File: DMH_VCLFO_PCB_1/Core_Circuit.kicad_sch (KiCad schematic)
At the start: 0 parts

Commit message: schematic design in progress
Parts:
- added C5: 1uF, Capacitor_THT:C_Disc_D4.3mm_W1.9mm_P5.00mm, symbol Device:C
- added C6: 100nF, Capacitor_THT:C_Disc_D4.3mm_W1.9mm_P5.00mm, symbol Device:C
- added C7: 10nF, Capacitor_THT:C_Disc_D4.3mm_W1.9mm_P5.00mm, symbol Device:C
- added C8: 100pF, Capacitor_THT:C_Disc_D4.3mm_W1.9mm_P5.00mm, symbol Device:C
- added D3, D4: 1N4148, Diode_THT:D_DO-35_SOD27_P7.62mm_Horizontal, symbol Diode:1N4148
- added J1, J2: TS_Jack_6.35mm_Sw, SynthStuff:CUI_MJ-63052A, symbol SynthStuff:TS_Jack_6.35mm_Sw
- added Q1: BS170, Package_TO_SOT_THT:TO-92_Inline, symbol Transistor_FET:BS170
- added Q2, Q3: BC548, Package_TO_SOT_THT:TO-92L_Inline_Wide, symbol Transistor_BJT:BC548
- added R1: 270R, Resistor_THT:R_Axial_DIN0207_L6.3mm_D2.5mm_P7.62mm_Horizontal, symbol Device:R_US
- added R10, R16, R8, R9: 51k, Resistor_THT:R_Axial_DIN0207_L6.3mm_D2.5mm_P7.62mm_Horizontal, symbol Device:R_US
- added R11, R17: 47k, Resistor_THT:R_Axial_DIN0207_L6.3mm_D2.5mm_P7.62mm_Horizontal, symbol Device:R_US
- added R12, R14, R15: 10k, Resistor_THT:R_Axial_DIN0207_L6.3mm_D2.5mm_P7.62mm_Horizontal, symbol Device:R_US
- added R13: 3k9, Resistor_THT:R_Axial_DIN0207_L6.3mm_D2.5mm_P7.62mm_Horizontal, symbol Device:R_US
- added R18, R19, R2, R20, R4, R5, R6, R7: 100k, Resistor_THT:R_Axial_DIN0207_L6.3mm_D2.5mm_P7.62mm_Horizontal, symbol Device:R_US
- added R3: 33k, Resistor_THT:R_Axial_DIN0207_L6.3mm_D2.5mm_P7.62mm_Horizontal, symbol Device:R_US
- added RV1: 50k, Potentiometer_THT:Potentiometer_Bourns_3296X_Horizontal, symbol Device:R_Potentiometer_Trim_US
- added RV1, RV2: B100k, SynthStuff:Potentiometer_TT_P110KH1, symbol Device:R_Potentiometer_US
- added SW1: SW_SPDT, symbol Switch:SW_SPDT
- added U1: TL074, Package_DIP:DIP-14_W7.62mm_Socket, symbol Amplifier_Operational:TL074
- added U2, U7: TL072, Package_DIP:DIP-8_W7.62mm_Socket, symbol Amplifier_Operational:TL072
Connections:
- new net: Q1.1 (D), R9.2
- new net: Q1.2 (G), R13.1, R14.1
- new net: C7.1, J2.T, R11.1
- new net: R15.1, R16.1, U1.5 (+)
- new net: C5.2, C6.2, R18.1, R19.1, U1.1, U1.6 (-)
- new net: D4.2 (A), R14.2, R15.2, U1.7
- new net: R2.1, R4.1, U1.13 (-)
- new net: R4.2, R7.1, R8.1, U1.14
- new net: D4.1 (K), R17.1
- new net: Q3.2 (B), R17.2
- new net: C7.2, D3.1 (K), R12.1
- new net: Q2.2 (B), R12.2
- new net: R10.1, R8.2, U1.3 (+)
- new net: Q3.1 (C), R18.2, U2.3 (+)
- new net: C6.1, Q2.1 (C), R7.2, R9.1, SW1.2 (B), U1.2 (-)
- new net: J1.T, R3.1, RV2.3
- new net: R3.2, RV1.1, U7.2 (-)
- new net: R6.2, RV1.2, RV1.3, U7.1
- new net: R5.2, R6.1, U1.12 (+)
- new net: R1.1, RV1.1
- new net: R5.1, RV1.2
- new net: C5.1, SW1.1 (A)
- new net: C8.1, R19.2, R20.1, U2.2 (-)
- new net: C8.2, R20.2, U2.1
- new net: RV2.2, U7.3 (+)
- new net +12V: RV1.3
- new net GND: D3.2 (A), J1.S, J2.S, Q1.3 (S), Q2.3 (E), Q3.3 (E), R1.2, R10.2, R11.2, R13.2, R16.2, R2.2, RV2.1
- no-connect marks 0 -> 1

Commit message: Update Core_Circuit.kicad_sch
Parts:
- added R21, R22: 10k, Resistor_THT:R_Axial_DIN0207_L6.3mm_D2.5mm_P7.62mm_Horizontal, symbol Device:R_US
- added R23, R24: 100k, Resistor_THT:R_Axial_DIN0207_L6.3mm_D2.5mm_P7.62mm_Horizontal, symbol Device:R_US
- added R25, R26, R27, R28: 1k, Resistor_THT:R_Axial_DIN0207_L6.3mm_D2.5mm_P7.62mm_Horizontal, symbol Device:R_US
- added unit 3 of U2
- added unit 4 of U2
- added unit 2 of U2
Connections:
- net GND: now also R24.1, U2.12 (+)
- net at C5.2, C6.2, R18.1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: now also U2.10 (+)
- net at D4.2 (A), R14.2, R15.2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: now also R23.1
- net at C8.2, R20.2, U2.1: now also R21.1, R26.1
- new net: R22.2, R27.1, U2.14
- new net: R21.2, R22.1, U2.13 (-)
- new net: R25.1, U2.8, U2.9 (-)
- new net: R23.2, R24.2, U2.5 (+)
- new net: R28.1, U2.6 (-), U2.7

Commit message: Update Core_Circuit.kicad_sch
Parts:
- added J3: TS_Jack_6.35mm_Sw, SynthStuff:CUI_MJ-63052A, symbol SynthStuff:TS_Jack_6.35mm_Sw
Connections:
- net at R26.2: now also J3.T
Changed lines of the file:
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@@
+	(wire
+		(pts
+			(xy 264.16 38.1) (xy 271.78 38.1)
+		)
+		(stroke
+			(width 0)
+			(type default)
+		)
+	)
 	(wire
 		(pts
@@
 					(unit 1)
 				)
+			)
+		)
+	)
+	(symbol
+		(lib_id "SynthStuff:TS_Jack_6.35mm_Sw")
+		(at 276.86 38.1 180)
+		(unit 1)
+		(exclude_from_sim no)
+		(in_bom yes)
+		(on_board yes)
+		(dnp no)
+		(property "Reference" "J3"
+			(at 276.86 31.496 0)
+			(effects
+				(font
+					(size 1.27 1.27)
+				)
+			)
+		)
+		(property "Value" "TS_Jack_6.35mm_Sw"
+			(at 277.495 44.45 0)
+			(effects
+				(font
+					(size 1.27 1.27)
+				)
+				(hide yes)
+			)
+		)
+		(property "Footprint" "SynthStuff:CUI_MJ-63052A"
+			(at 276.86 38.1 0)
+			(effects
+				(font
+					(size 1.27 1.27)
+				)
+				(hide yes)
+			)
+		)
+		(property "Datasheet" "~"
+			(at 276.86 38.1 0)
+			(effects
+				(font
+					(size 1.27 1.27)
+				)
+				(hide yes)
+			)
+		)
+		(property "Description" "Audio Jack, 2 Poles (Mono / TS), Switched T Pole (Normalling), 6.35mm, 1/4inch"
+			(at 276.86 38.1 0)
+			(effects
+				(font
+					(size 1.27 1.27)
+				)
+				(hide yes)
+			)
+		)
+		(property "Function" "Out A Saw"
+			(at 276.86 43.688 0)
+			(effects
+				(font
+					(size 1.27 1.27)
+					(thickness 0.254)
+					(bold yes)
+					(italic yes)
+				)
+			)
+		)
+		(pin "S"
+		)
+		(pin "T"
+		)
+		(pin "TN"
+		)
+		(instances
+			(project "DMH_VCLFO_PCB_1"
+				(path "/58f4306d-5387-4983-bb08-41a2313fd315/7ad2d702-dfb7-4d49-a82d-34430dd5948f"
+					(reference "J3")
+					(unit 1)
+				)

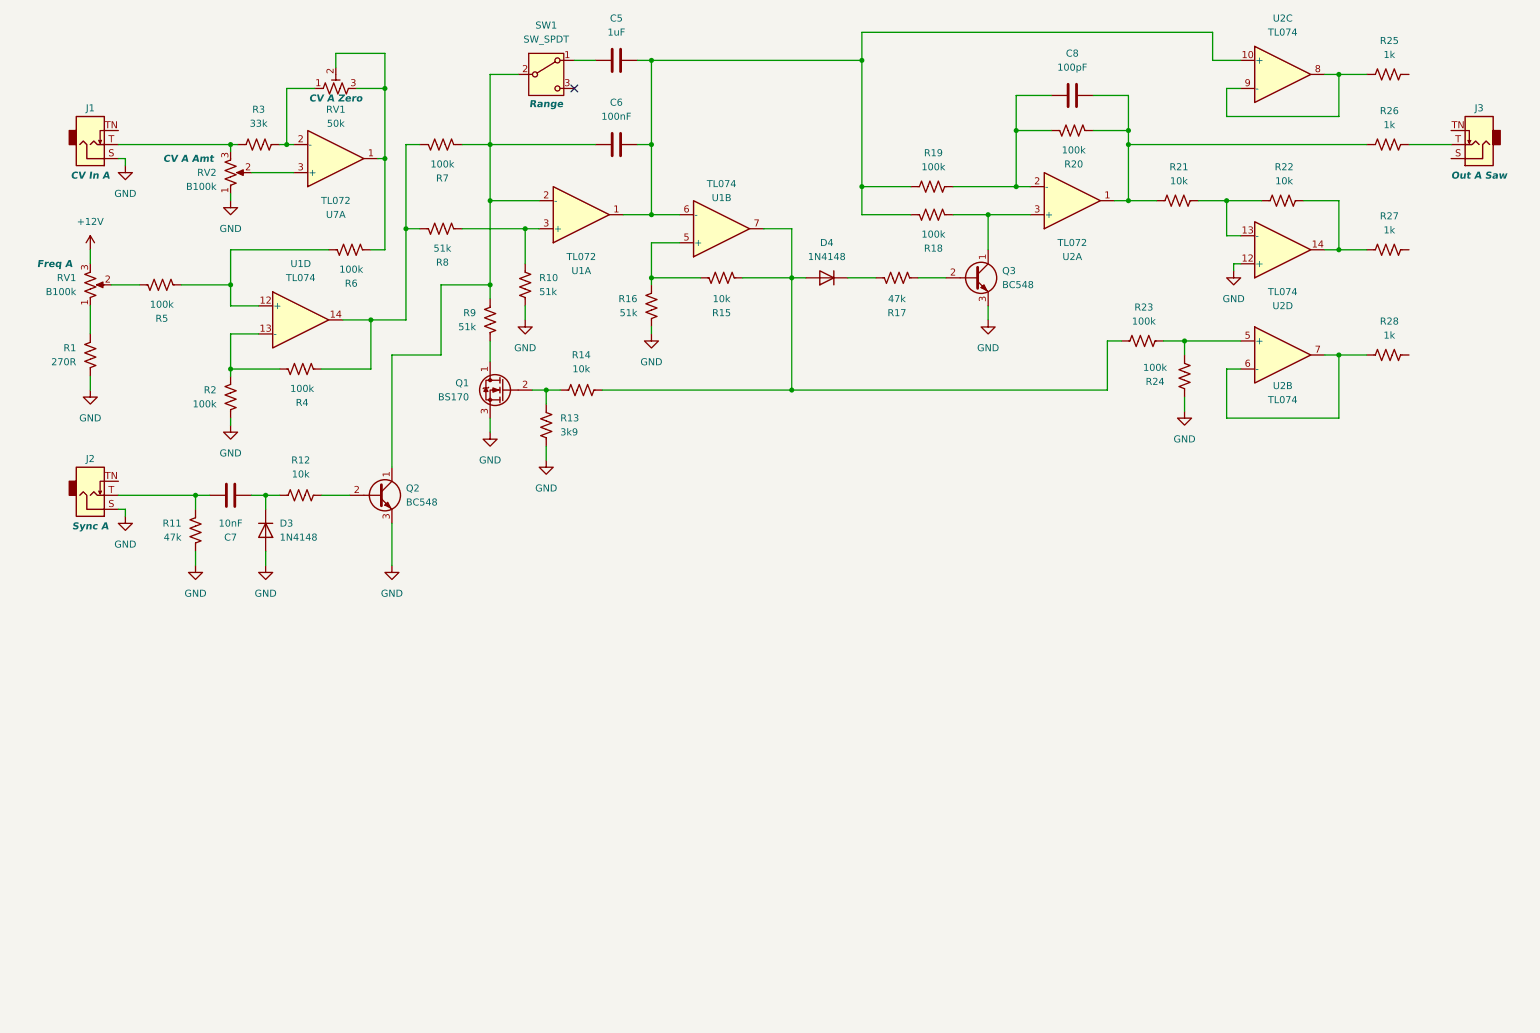
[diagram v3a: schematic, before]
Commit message: Completed basic core circuit schematic
... escept for polarization switch
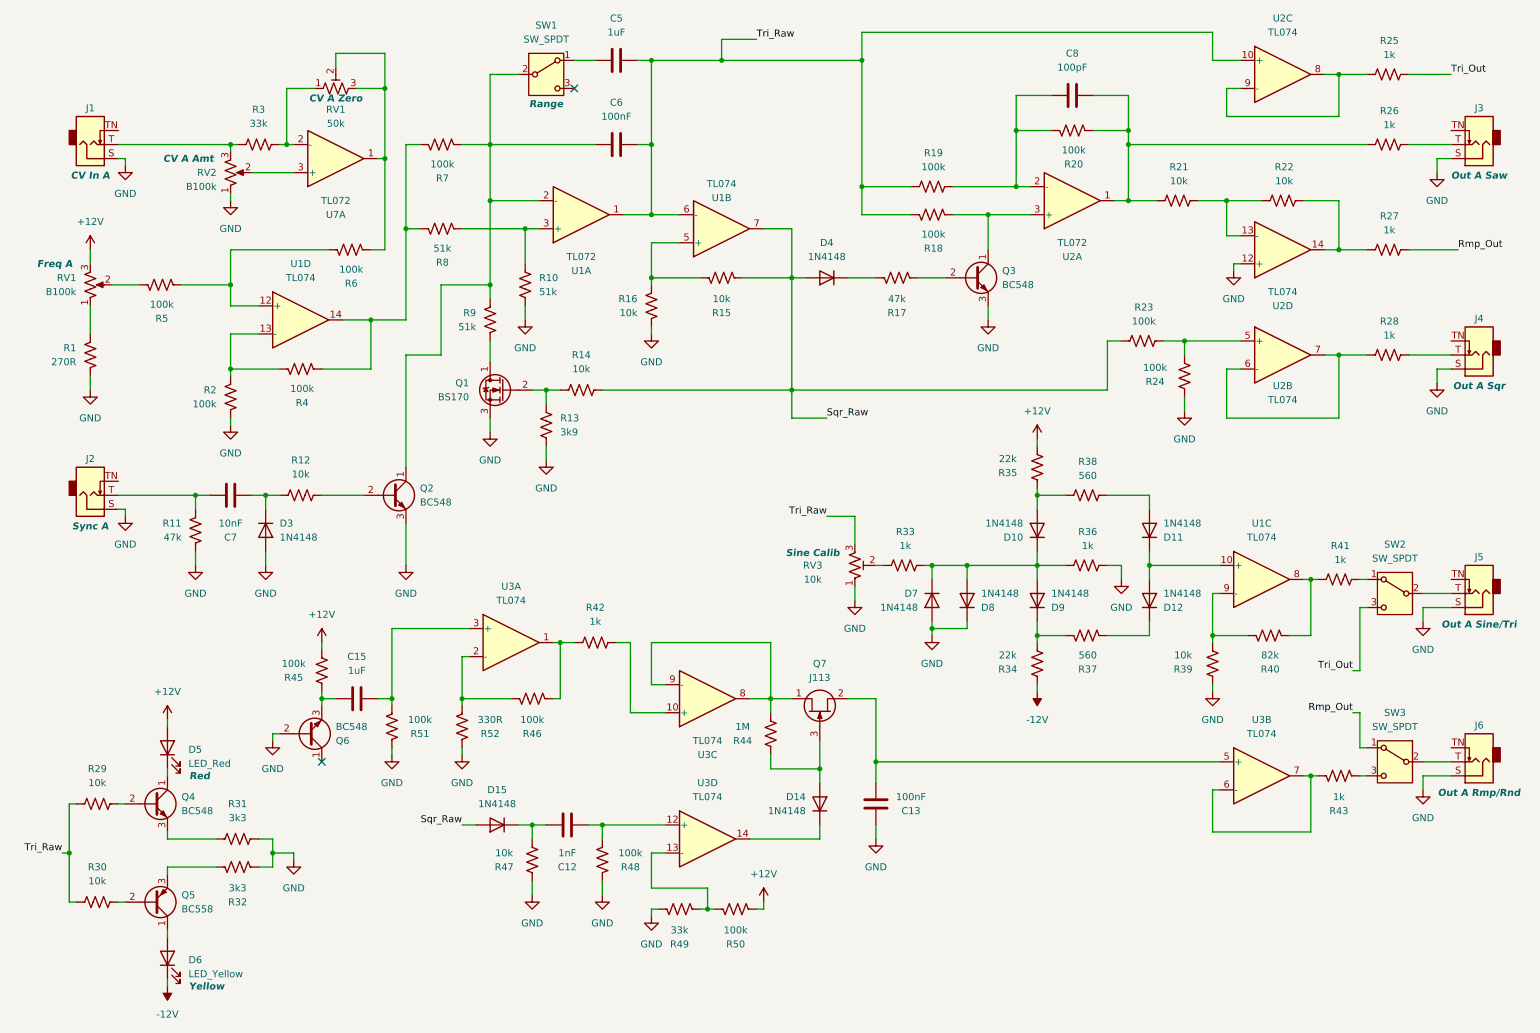
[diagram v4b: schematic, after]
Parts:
- added C12: 1nF, Capacitor_THT:C_Disc_D4.3mm_W1.9mm_P5.00mm, symbol Device:C
- added C13: 100nF, Capacitor_THT:C_Disc_D4.3mm_W1.9mm_P5.00mm, symbol Device:C
- added C15: 1uF, Capacitor_THT:C_Disc_D4.3mm_W1.9mm_P5.00mm, symbol Device:C
- added D10, D11, D12, D7, D8, D9: 1N4148, Diode_THT:D_DO-35_SOD27_P7.62mm_Horizontal, symbol Diode:1N4148
- added D14, D15: 1N4148, Diode_THT:D_DO-35_SOD27_P7.62mm_Horizontal, symbol Device:D
- added D5: LED_Red, LED_THT:LED_D3.0mm, symbol Device:LED
- added D6: LED_Yellow, LED_THT:LED_D3.0mm, symbol Device:LED
- added J4, J5, J6: TS_Jack_6.35mm_Sw, SynthStuff:CUI_MJ-63052A, symbol SynthStuff:TS_Jack_6.35mm_Sw
- added Q4: BC548, Package_TO_SOT_THT:TO-92L_Inline_Wide, symbol Transistor_BJT:BC548
- added Q5: BC558, Package_TO_SOT_THT:TO-92L_Inline_Wide, symbol Transistor_BJT:BC558
- added Q6: BC548, Package_TO_SOT_THT:TO-92_Inline_Wide, symbol Transistor_BJT:BC548
- added Q7: J113, Package_TO_SOT_THT:TO-92L_Inline, symbol Transistor_FET:MMBFJ113
- added R29, R30, R39, R47: 10k, Resistor_THT:R_Axial_DIN0207_L6.3mm_D2.5mm_P7.62mm_Horizontal, symbol Device:R_US
- added R31, R32: 3k3, Resistor_THT:R_Axial_DIN0207_L6.3mm_D2.5mm_P7.62mm_Horizontal, symbol Device:R_US
- added R33, R36, R41, R42, R43: 1k, Resistor_THT:R_Axial_DIN0207_L6.3mm_D2.5mm_P7.62mm_Horizontal, symbol Device:R_US
- added R34, R35: 22k, Resistor_THT:R_Axial_DIN0207_L6.3mm_D2.5mm_P7.62mm_Horizontal, symbol Device:R_US
- added R37, R38: 560, Resistor_THT:R_Axial_DIN0207_L6.3mm_D2.5mm_P7.62mm_Horizontal, symbol Device:R_US
- added R40: 82k, Resistor_THT:R_Axial_DIN0207_L6.3mm_D2.5mm_P7.62mm_Horizontal, symbol Device:R_US
- added R44: 1M, Resistor_THT:R_Axial_DIN0207_L6.3mm_D2.5mm_P7.62mm_Horizontal, symbol Device:R_US
- added R45, R46, R48, R50, R51: 100k, Resistor_THT:R_Axial_DIN0207_L6.3mm_D2.5mm_P7.62mm_Horizontal, symbol Device:R_US
- added R49: 33k, Resistor_THT:R_Axial_DIN0207_L6.3mm_D2.5mm_P7.62mm_Horizontal, symbol Device:R_US
- added R52: 330R, Resistor_THT:R_Axial_DIN0207_L6.3mm_D2.5mm_P7.62mm_Horizontal, symbol Device:R_US
- added RV3: 10k, Potentiometer_THT:Potentiometer_Bourns_3296W_Vertical, symbol Device:R_Potentiometer_Trim_US
- added SW2, SW3: SW_SPDT, symbol Switch:SW_SPDT
- added unit 3 of U1
- added U3: TL074, Package_DIP:DIP-14_W7.62mm_Socket, symbol Amplifier_Operational:TL074
- R16: value 51k -> 10k
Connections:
- net +12V: now also D5.2 (A), R35.2, R45.1, R50.1
- net GND: now also J3.S, C13.2, D7.2 (A), D8.1 (K), J4.S, J5.S, J6.S, Q6.2 (B), R31.2, R32.2, R36.2, R39.1, R47.2, R48.2, R49.2, R51.2, R52.2, RV3.1
- net Tri_Raw: now reaches C5.2, C6.2, R18.1, R19.1, U1.1, U1.6 (-), U2.10 (+)
- net Tri_Raw: now also R29.1, R30.1, RV3.3
- net Sqr_Raw: now reaches D4.2 (A), R14.2, R15.2, R23.1, U1.7
- net Sqr_Raw: now also D15.2 (A)
- net Rmp_Out: now reaches R27.2
- net Rmp_Out: now also SW3.1 (A)
- net Tri_Out: now reaches R25.2
- net Tri_Out: now also SW2.3 (C)
- net at R28.2: now also J4.T
- new net: D10.1 (K), D7.1 (K), D8.2 (A), D9.2 (A), R33.2, R36.1
- new net: D10.2 (A), R35.1, R38.1
- new net: D14.1 (K), U3.14
- new net: D14.2 (A), Q7.3 (G), R44.2
- new net: D11.2 (A), R38.2
- new net: J6.T, SW3.2 (B)
- new net: R43.1, SW3.3 (C)
- new net: R33.1, RV3.2
- new net: R42.2, R46.1, U3.1
- new net: R46.2, R52.1, U3.2 (-)
- new net: R42.1, U3.10 (+)
- new net: Q7.1 (D), R44.1, U3.8, U3.9 (-)
- new net: D9.1 (K), R34.2, R37.1
- new net: C12.1, R48.1, U3.12 (+)
- new net: R49.1, R50.2, U3.13 (-)
- new net: Q4.2 (B), R29.2
- new net: D11.1 (K), D12.2 (A), U1.10 (+)
- new net: R40.2, R41.1, U1.8
- new net: R39.2, R40.1, U1.9 (-)
- new net: Q5.3 (E), R32.1
- new net: C15.1, Q6.3 (E), R45.2
- new net: R41.2, SW2.1 (A)
- new net: Q5.2 (B), R30.2
- new net: D5.1 (K), Q4.1 (C)
- new net: Q4.3 (E), R31.1
- new net: R43.2, U3.6 (-), U3.7
- new net: J5.T, SW2.2 (B)
- new net: C12.2, D15.1 (K), R47.1
- new net: D6.2 (A), Q5.1 (C)
- new net: C15.2, R51.1, U3.3 (+)
- new net: C13.1, Q7.2 (S), U3.5 (+)
- new net: D12.1 (K), R37.2
- new net -12V: D6.1 (K), R34.1
- no-connect marks 1 -> 2
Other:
- moved on the sheet: Q2

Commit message: Ready for breadboarding
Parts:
- removed J1, J2, J3, J4, J5, J6: TS_Jack_6.35mm_Sw, SynthStuff:CUI_MJ-63052A, symbol SynthStuff:TS_Jack_6.35mm_Sw
- removed R1: 270R, Resistor_THT:R_Axial_DIN0207_L6.3mm_D2.5mm_P7.62mm_Horizontal, symbol Device:R_US
- removed R25, R26, R27, R28, R41, R42, R43: 1k, Resistor_THT:R_Axial_DIN0207_L6.3mm_D2.5mm_P7.62mm_Horizontal, symbol Device:R_US
- removed R3: 33k, Resistor_THT:R_Axial_DIN0207_L6.3mm_D2.5mm_P7.62mm_Horizontal, symbol Device:R_US
- removed RV1: 50k, Potentiometer_THT:Potentiometer_Bourns_3296X_Horizontal, symbol Device:R_Potentiometer_Trim_US
- removed RV1, RV2: B100k, SynthStuff:Potentiometer_TT_P110KH1, symbol Device:R_Potentiometer_US
- removed SW1, SW2, SW3: SW_SPDT, symbol Switch:SW_SPDT
- removed unit 1 of U1
- removed unit 4 of U2
- removed unit 1 of U2
- removed unit 3 of U3
- removed U7: TL072, Package_DIP:DIP-8_W7.62mm_Socket, symbol Amplifier_Operational:TL072
- added unit 1 of U10
- added unit 4 of U11
- added unit 1 of U11
- R39: renamed from R11; value 47k -> 100k
- U10: renamed from U1; footprint (none) -> Package_DIP:DIP-14_W7.62mm_Socket
- renumbered C7 to C3, C15 to C4, C12 to C5, C5 to C6, C6 to C7, C13 to C8, C8 to C9, D4 to D10, D7 to D11, D8 to D12, D10 to D13, D9 to D14, D11 to D15, D12 to D16, D3 to D7, D15 to D8, D14 to D9, Q4 to Q1, Q5 to Q2, Q2 to Q3, Q6 to Q4, Q1 to Q5, Q7 to Q6, Q3 to Q7, R29 to R35, R30 to R36, R6 to R37, R5 to R38, R2 to R40, R31 to R41, R32 to R42, R4 to R43, R12 to R44, R7 to R45, R8 to R46, R45 to R47, R9 to R48, R10 to R49, R51 to R50, R47 to R51, R13 to R52, R14 to R53, R52 to R54, R48 to R55, R16 to R56, R49 to R57, R46 to R58, R15 to R59, R50 to R60, R44 to R61, R17 to R62, R33 to R63, R19 to R64, R18 to R65, R35 to R66, R34 to R67, R20 to R68, R38 to R69, R36 to R70, R37 to R71, R23 to R72, R24 to R73, R21 to R74, R39 to R75, R40 to R76, R22 to R77, RV3 to RV4, U1 to U10, U2 to U11, U3 to U12, U1 to U12
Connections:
- net GND: now also U11.12 (+)
- net Tri_Raw: now also U10.1
- net Saw: now reaches C9.2, R68.2, R74.1
- net Saw: now also U11.1
- net Sync In: now reaches C3.1, R39.1
- net at R58.1, U12.1: now also Q6.1 (D), R61.1
- net Rmp: now reaches R77.2
- net Rmp: now also U11.14
- net at R74.2, R77.1: now also U11.13 (-)
- net at R46.2, R49.1: now also U10.3 (+)
- net at Q7.1 (C), R65.2: now also U11.3 (+)
- net Rng_Sw_2: now reaches C7.1, Q3.1 (C), R45.2, R48.1
- net Rng_Sw_2: now also U10.2 (-)
- net at R37.2: now also R38.2, U10.12 (+)
- net Pot In: now reaches R38.1
- net Tri: now reaches U11.8, U11.9 (-)
- net Rng_Sw_1: now reaches C6.1
- net Sin: now reaches R76.2, U12.8
- net Rnd: now reaches U12.6 (-), U12.7
- net at C9.1, R64.2, R68.1: now also U11.2 (-)
- net Sqr: now reaches U11.6 (-), U11.7
- new net CV In: R37.1
- no-connect marks 2 -> 1
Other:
- note added: "Needs simulation"
- note added: "Was 47k"
- moved on the sheet: C3, C4, C5, D5, D6, D7, D8, D9, Q1, Q2, Q3, Q4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
